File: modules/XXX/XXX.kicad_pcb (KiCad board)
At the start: 2 copper layers, 160 x 100 mm, 15 parts, among them J1 CardConnector, SW1 AS13AP, SW2 AS13AP, SW3 AS13AP

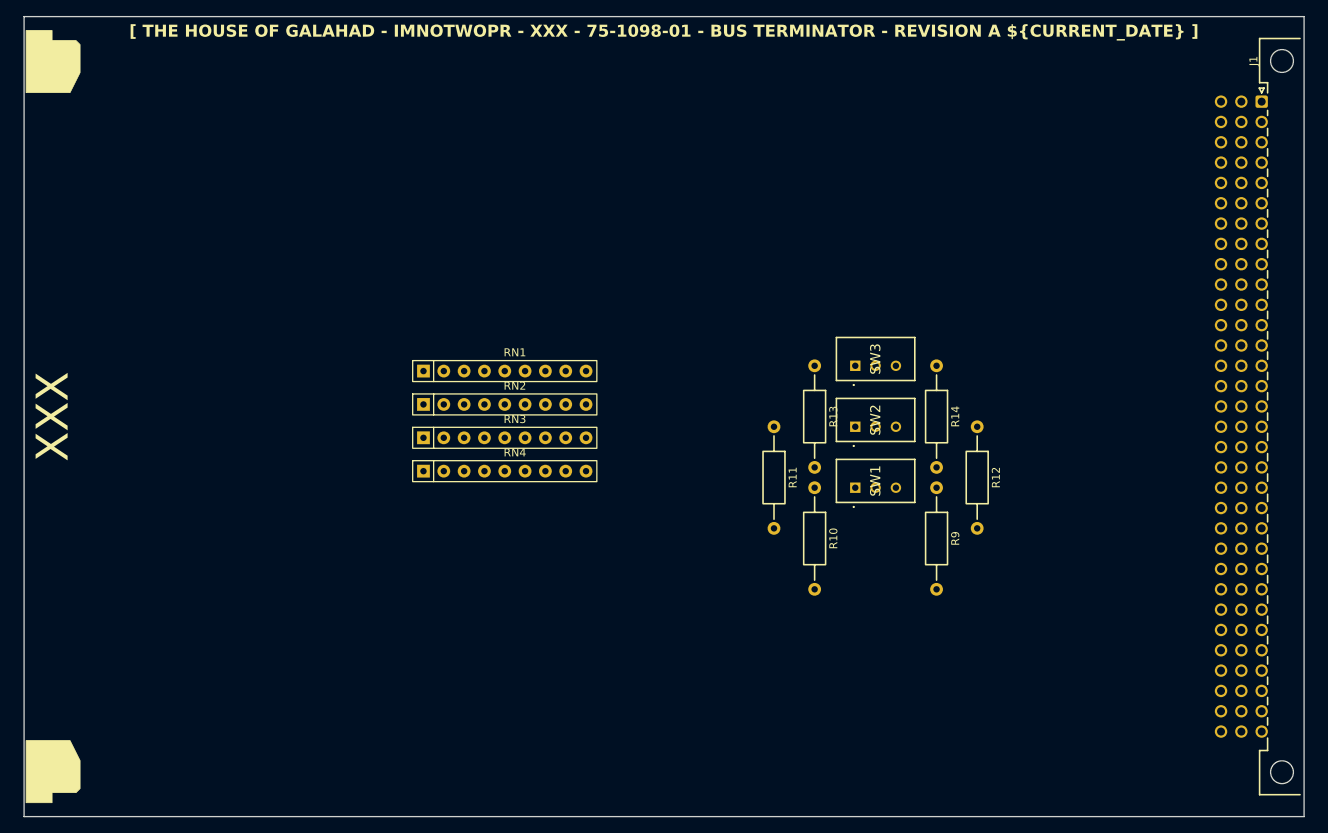
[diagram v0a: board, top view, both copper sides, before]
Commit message: fixed level shifter footprint width
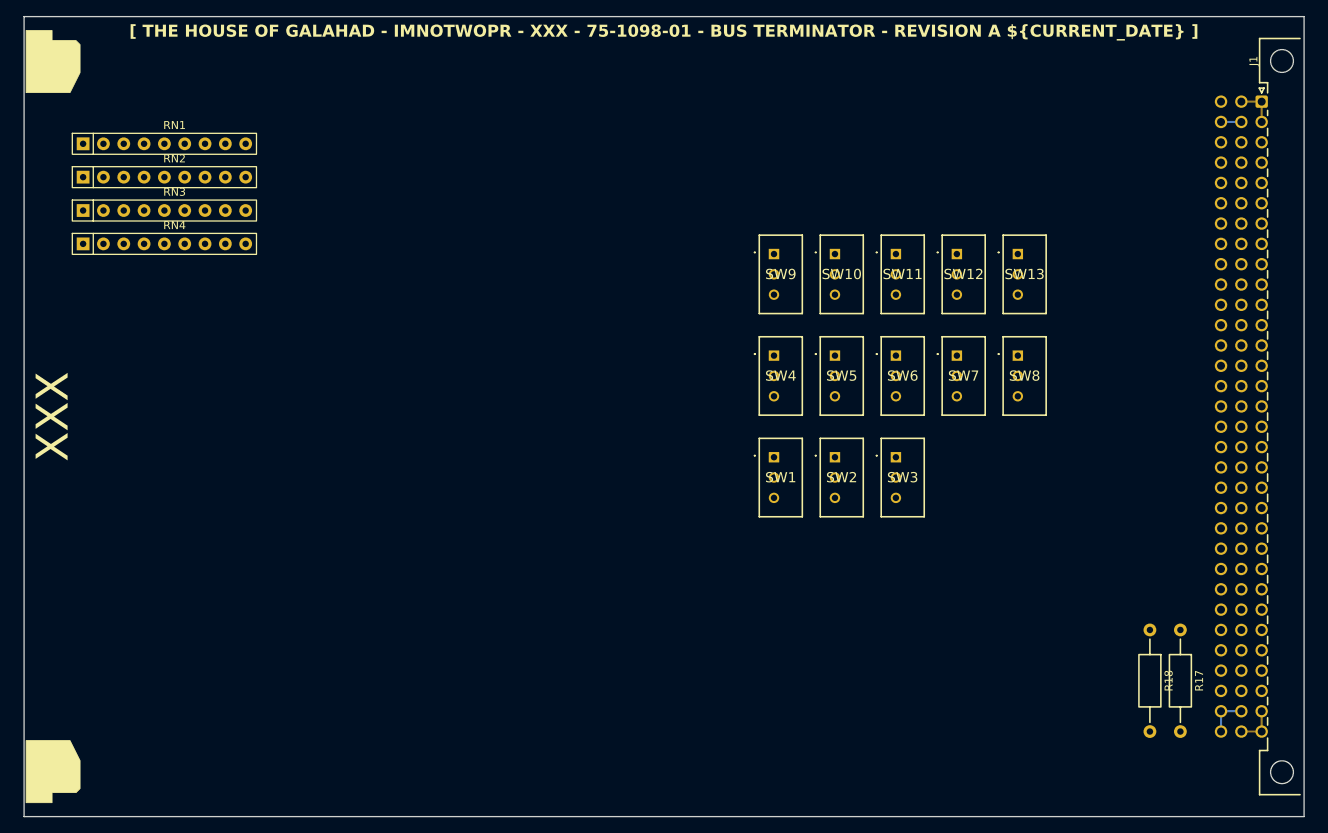
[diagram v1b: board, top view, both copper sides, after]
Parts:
- removed R10, R11, R12, R13, R14, R9: 10k, IMNOTWOPR:R_Axial_DIN0207_P400mil
- added R17: 10k, IMNOTWOPR:R_Axial_DIN0207_P400mil, F.Cu at (199.5, 128.0)
- added R18: 10k, IMNOTWOPR:R_Axial_DIN0207_P400mil, F.Cu at (195.7, 128.0)
- added SW10: AS13AP, IMNOTWOPR:AS13AP, F.Cu at (156.4, 74.7)
- added SW11: AS13AP, IMNOTWOPR:AS13AP, F.Cu at (164.0, 74.7)
- added SW12: AS13AP, IMNOTWOPR:AS13AP, F.Cu at (171.6, 74.7)
- added SW13: AS13AP, IMNOTWOPR:AS13AP, F.Cu at (179.2, 74.7)
- added SW4: AS13AP, IMNOTWOPR:AS13AP, F.Cu at (148.7, 87.4)
- added SW5: AS13AP, IMNOTWOPR:AS13AP, F.Cu at (156.4, 87.4)
- added SW6: AS13AP, IMNOTWOPR:AS13AP, F.Cu at (164.0, 87.4)
- added SW7: AS13AP, IMNOTWOPR:AS13AP, F.Cu at (171.6, 87.4)
- added SW8: AS13AP, IMNOTWOPR:AS13AP, F.Cu at (179.2, 87.4)
- added SW9: AS13AP, IMNOTWOPR:AS13AP, F.Cu at (148.7, 74.7)
- moved RN2 51.2 mm to (62.4, 65.1)
- moved RN3 51.2 mm to (62.4, 69.2)
- moved RN1 51.2 mm to (62.4, 60.9)
- moved RN4 51.2 mm to (62.4, 73.4)
- moved SW3 12.5 mm to (164.0, 100.1), turned to 0 degrees
- moved SW1 10.9 mm to (148.7, 100.1), turned to 0 degrees
- moved SW2 4.58 mm to (156.4, 100.1), turned to 0 degrees
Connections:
- J1 pad c10: unconnected-(J1C-BUSREQ3-Padc10) -> Net-(J1C-BUSREQ3)
- J1 pad c11: unconnected-(J1C-BUSREQ4-Padc11) -> Net-(J1C-BUSREQ4)
- J1 pad c13: unconnected-(J1C-BUSGNT0-Padc13) -> Net-(J1C-BUSGNT0)
- J1 pad c14: unconnected-(J1C-BUSGNT1-Padc14) -> Net-(J1C-BUSGNT1)
- J1 pad c15: unconnected-(J1C-BUSGNT2-Padc15) -> Net-(J1C-BUSGNT2)
- J1 pad c16: unconnected-(J1C-BUSGNT3-Padc16) -> Net-(J1C-BUSGNT3)
- J1 pad c17: unconnected-(J1C-BUSGNT4-Padc17) -> Net-(J1C-BUSGNT4)
- J1 pad c22: unconnected-(J1C-I^{2}C_SCL-Padc22) -> Net-(J1C-I^{2}C_SCL)
- J1 pad c23: unconnected-(J1C-I^{2}C_SDA-Padc23) -> Net-(J1C-I^{2}C_SDA)
- J1 pad c7: unconnected-(J1C-BUSREQ0-Padc7) -> Net-(J1C-BUSREQ0)
- J1 pad c8: unconnected-(J1C-BUSREQ1-Padc8) -> Net-(J1C-BUSREQ1)
- J1 pad c9: unconnected-(J1C-BUSREQ2-Padc9) -> Net-(J1C-BUSREQ2)
- SW1 pad 1: Net-(R10-Pad1) -> unconnected-(SW1-Pad1)
- SW1 pad 3: Net-(SW1-4) -> unconnected-(SW1-4-Pad3)
- SW2 pad 1: Net-(R11-Pad1) -> unconnected-(SW2-Pad1)
- SW2 pad 3: Net-(SW2-4) -> unconnected-(SW2-4-Pad3)
- SW3 pad 1: Net-(R13-Pad1) -> unconnected-(SW3-Pad1)
- SW3 pad 3: Net-(SW3-4) -> unconnected-(SW3-4-Pad3)
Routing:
- net +5V: track 0.00 -> 10.2 mm
- net GND: track 0.00 -> 7.62 mm

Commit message: xxx bus terminator card
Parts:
- removed R17, R18: 10k, IMNOTWOPR:R_Axial_DIN0207_P400mil
- removed RN4: 10k, Resistor_THT:R_Array_SIP9
- removed SW1, SW2, SW3, SW4, SW5, SW6, SW7, SW8: AS13AP, IMNOTWOPR:AS13AP
- added JP1: SDA_PU, IMNOTWOPR:Jumper_1x02, F.Cu at (164.0, 129.3)
- added JP2: SCL_PU, IMNOTWOPR:Jumper_1x02, F.Cu at (171.6, 129.3)
- added R1: 4k7, IMNOTWOPR:R_Axial_DIN0207_P400mil, F.Cu at (164.0, 117.9)
- added R2: 4k7, IMNOTWOPR:R_Axial_DIN0207_P400mil, F.Cu at (171.6, 115.3)
- added R3: 1k, IMNOTWOPR:R_Axial_DIN0207_P400mil, F.Cu at (158.9, 111.5)
- added R4: 1k, IMNOTWOPR:R_Axial_DIN0207_P400mil, F.Cu at (153.8, 120.4)
- added R5: 47k, IMNOTWOPR:R_Axial_DIN0207_P400mil, F.Cu at (161.4, 95.0)
- added R6: 47k, IMNOTWOPR:R_Axial_DIN0207_P400mil, F.Cu at (166.5, 97.5)
- added R7: 47k, IMNOTWOPR:R_Axial_DIN0207_P400mil, F.Cu at (171.6, 100.1)
- added RN6: 47k, Resistor_THT:R_Array_SIP6, F.Cu at (197.0, 106.4)
- added RN7: 47k, Resistor_THT:R_Array_SIP6, F.Cu at (197.0, 68.3)
- added RN8: 47k, Resistor_THT:R_Array_SIP6, F.Cu at (197.0, 83.6)
- RN1: value 10k -> 47k
- RN3: value 10k -> 4k7
- moved RN1 141.0 mm to (191.9, 116.6), turned to -90 degrees
- moved SW10 39.2 mm to (120.8, 58.2)
- moved SW11 39.2 mm to (128.4, 58.2)
- moved SW12 39.2 mm to (136.0, 58.2)
- moved SW13 39.2 mm to (143.7, 58.2)
- moved SW9 39.2 mm to (113.2, 58.2)
- moved RN2 26.3 mm to (88.1, 70.3)
- moved RN3 26.3 mm to (88.1, 74.4)
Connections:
- J1 pad a10: Net-(J1A-A_{14}) -> unconnected-(J1A-A_{14}-Pada10)
- J1 pad a11: Net-(J1A-A_{15}) -> unconnected-(J1A-A_{15}-Pada11)
- J1 pad a12: Net-(J1A-A_{16}) -> unconnected-(J1A-A_{16}-Pada12)
- J1 pad a13: Net-(J1A-A_{17}) -> unconnected-(J1A-A_{17}-Pada13)
- J1 pad a14: Net-(J1A-A_{18}) -> unconnected-(J1A-A_{18}-Pada14)
- J1 pad a15: Net-(J1A-A_{19}) -> unconnected-(J1A-A_{19}-Pada15)
- J1 pad a16: Net-(J1A-A_{20}) -> unconnected-(J1A-A_{20}-Pada16)
- J1 pad a17: Net-(J1A-A_{21}) -> unconnected-(J1A-A_{21}-Pada17)
- J1 pad a18: Net-(J1A-A_{22}) -> unconnected-(J1A-A_{22}-Pada18)
- J1 pad a19: Net-(J1A-A_{23}) -> unconnected-(J1A-A_{23}-Pada19)
- J1 pad a20: unconnected-(J1A-ABORT-Pada20) -> #ABORT
- J1 pad a25: unconnected-(J1A-HALT?-Pada25) -> #HALT
- J1 pad a26: unconnected-(J1A-IRQ_{4}-Pada26) -> #IRQ4
- J1 pad a27: unconnected-(J1A-IRQ_{5}-Pada27) -> #IRQ5
- J1 pad a28: unconnected-(J1A-IRQ_{6}-Pada28) -> #IRQ6
- J1 pad a29: unconnected-(J1A-IRQ_{7}-Pada29) -> #IRQ7
- J1 pad a4: Net-(J1A-A_{8}) -> unconnected-(J1A-A_{8}-Pada4)
- J1 pad a5: Net-(J1A-A_{9}) -> unconnected-(J1A-A_{9}-Pada5)
- J1 pad a6: Net-(J1A-A_{10}) -> unconnected-(J1A-A_{10}-Pada6)
- J1 pad a7: Net-(J1A-A_{11}) -> unconnected-(J1A-A_{11}-Pada7)
- J1 pad a8: Net-(J1A-A_{12}) -> unconnected-(J1A-A_{12}-Pada8)
- J1 pad a9: Net-(J1A-A_{13}) -> unconnected-(J1A-A_{13}-Pada9)
- J1 pad b10: Net-(J1B-A_{6}) -> unconnected-(J1B-A_{6}-Padb10)
- J1 pad b11: Net-(J1B-A_{7}) -> unconnected-(J1B-A_{7}-Padb11)
- J1 pad b12: unconnected-(J1B-RESET-Padb12) -> #RESET
- J1 pad b16: Net-(J1B-D_{0}) -> unconnected-(J1B-D_{0}-Padb16)
- J1 pad b17: Net-(J1B-D_{1}) -> unconnected-(J1B-D_{1}-Padb17)
- J1 pad b18: Net-(J1B-D_{2}) -> unconnected-(J1B-D_{2}-Padb18)
- J1 pad b19: Net-(J1B-D_{3}) -> unconnected-(J1B-D_{3}-Padb19)
- J1 pad b20: Net-(J1B-D_{4}) -> unconnected-(J1B-D_{4}-Padb20)
- J1 pad b21: Net-(J1B-D_{5}) -> unconnected-(J1B-D_{5}-Padb21)
- J1 pad b22: Net-(J1B-D_{6}) -> unconnected-(J1B-D_{6}-Padb22)
- J1 pad b23: Net-(J1B-D_{7}) -> unconnected-(J1B-D_{7}-Padb23)
- J1 pad b24: unconnected-(J1B-IRQ-Padb24) -> #IRQ
- J1 pad b25: unconnected-(J1B-NMI-Padb25) -> #NMI
- J1 pad b26: unconnected-(J1B-IRQ_{0}-Padb26) -> #IRQ0
- J1 pad b27: unconnected-(J1B-IRQ_{1}-Padb27) -> #IRQ1
- J1 pad b28: unconnected-(J1B-IRQ_{2}-Padb28) -> #IRQ2
- J1 pad b29: unconnected-(J1B-IRQ_{3}-Padb29) -> #IRQ3
- J1 pad b4: Net-(J1B-A_{0}) -> unconnected-(J1B-A_{0}-Padb4)
- J1 pad b5: Net-(J1B-A_{1}) -> unconnected-(J1B-A_{1}-Padb5)
- J1 pad b6: Net-(J1B-A_{2}) -> unconnected-(J1B-A_{2}-Padb6)
- J1 pad b7: Net-(J1B-A_{3}) -> unconnected-(J1B-A_{3}-Padb7)
- J1 pad b8: Net-(J1B-A_{4}) -> unconnected-(J1B-A_{4}-Padb8)
- J1 pad b9: Net-(J1B-A_{5}) -> unconnected-(J1B-A_{5}-Padb9)
- J1 pad c10: Net-(J1C-BUSREQ3) -> #BUSREQ3
- J1 pad c11: Net-(J1C-BUSREQ4) -> #BUSREQ4
- J1 pad c13: Net-(J1C-BUSGNT0) -> #BUSGNT0
- J1 pad c14: Net-(J1C-BUSGNT1) -> #BUSGNT1
- J1 pad c15: Net-(J1C-BUSGNT2) -> #BUSGNT2
- J1 pad c16: Net-(J1C-BUSGNT3) -> #BUSGNT3
- J1 pad c17: Net-(J1C-BUSGNT4) -> #BUSGNT4
- J1 pad c19: Net-(J1C-BANK0) -> #BANK0
- J1 pad c20: Net-(J1C-BANK1) -> #BANK1
- J1 pad c21: Net-(J1C-BANK2) -> #BANK2
- J1 pad c25: unconnected-(J1C-READY-Padc25) -> READY
- J1 pad c29: unconnected-(J1C-BE-Padc29) -> BE
- J1 pad c7: Net-(J1C-BUSREQ0) -> #BUSREQ0
- J1 pad c8: Net-(J1C-BUSREQ1) -> #BUSREQ1
- J1 pad c9: Net-(J1C-BUSREQ2) -> #BUSREQ2
- RN1 pad 1: Net-(RN1-common) -> +5V
- RN1 pad 2: Net-(J1A-A_{8}) -> #IRQ0
- RN1 pad 3: Net-(J1A-A_{9}) -> #IRQ4
- RN1 pad 4: Net-(J1A-A_{10}) -> #IRQ1
- RN1 pad 5: Net-(J1A-A_{11}) -> #IRQ5
- RN1 pad 6: Net-(J1A-A_{12}) -> #IRQ2
- RN1 pad 7: Net-(J1A-A_{13}) -> #IRQ6
- RN1 pad 8: Net-(J1A-A_{14}) -> #IRQ3
- RN1 pad 9: Net-(J1A-A_{15}) -> #IRQ7
- RN2 pad 1: Net-(RN1-common) -> +5V
- RN2 pad 2: Net-(J1A-A_{16}) -> unconnected-(RN2-R1-Pad2)
- RN2 pad 3: Net-(J1A-A_{17}) -> unconnected-(RN2-R2-Pad3)
- RN2 pad 4: Net-(J1A-A_{18}) -> unconnected-(RN2-R3-Pad4)
- RN2 pad 5: Net-(J1A-A_{19}) -> unconnected-(RN2-R4-Pad5)
- RN2 pad 6: Net-(J1A-A_{20}) -> unconnected-(RN2-R5-Pad6)
- RN2 pad 7: Net-(J1A-A_{21}) -> unconnected-(RN2-R6-Pad7)
- RN2 pad 8: Net-(J1A-A_{22}) -> unconnected-(RN2-R7-Pad8)
- RN2 pad 9: Net-(J1A-A_{23}) -> unconnected-(RN2-R8-Pad9)
- RN3 pad 1: Net-(RN1-common) -> GND
- RN3 pad 2: Net-(J1B-A_{0}) -> unconnected-(RN3-R1-Pad2)
- RN3 pad 3: Net-(J1B-A_{1}) -> unconnected-(RN3-R2-Pad3)
- RN3 pad 4: Net-(J1B-A_{2}) -> unconnected-(RN3-R3-Pad4)
- RN3 pad 5: Net-(J1B-A_{3}) -> unconnected-(RN3-R4-Pad5)
- RN3 pad 6: Net-(J1B-A_{4}) -> unconnected-(RN3-R5-Pad6)
- RN3 pad 7: Net-(J1B-A_{5}) -> unconnected-(RN3-R6-Pad7)
- RN3 pad 8: Net-(J1B-A_{6}) -> unconnected-(RN3-R7-Pad8)
- RN3 pad 9: Net-(J1B-A_{7}) -> unconnected-(RN3-R8-Pad9)
- SW10 pad 2: Net-(J1C-BUSREQ1) -> unconnected-(SW10-3-Pad2)
- SW11 pad 2: Net-(J1C-BUSREQ2) -> unconnected-(SW11-3-Pad2)
- SW12 pad 2: Net-(J1C-BUSREQ3) -> unconnected-(SW12-3-Pad2)
- SW13 pad 2: Net-(J1C-BUSREQ4) -> unconnected-(SW13-3-Pad2)
- SW9 pad 2: Net-(J1C-BUSREQ0) -> unconnected-(SW9-3-Pad2)
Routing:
- net #RESET: track 0.00 -> 30.7 mm
- net #IRQ7: track 0.00 -> 22.0 mm
- net #IRQ6: track 0.00 -> 20.9 mm
- net #IRQ5: track 0.00 -> 19.9 mm
- net #IRQ4: track 0.00 -> 18.8 mm
- net #IRQ3: track 0.00 -> 18.4 mm
- net #IRQ2: track 0.00 -> 17.3 mm
- net #IRQ1: track 0.00 -> 16.3 mm
- net #IRQ0: track 0.00 -> 16.3 mm
- net #ABORT: track 0.00 -> 15.9 mm
- net #HALT: track 0.00 -> 13.8 mm
- net #NMI: track 0.00 -> 11.2 mm
- net #IRQ: track 0.00 -> 11.2 mm
- net #BUSREQ4: track 0.00 -> 7.62 mm
- net #BUSREQ3: track 0.00 -> 7.62 mm
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
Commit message: pxx prototype card
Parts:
- removed SW10, SW11, SW12, SW13, SW9: AS13AP, IMNOTWOPR:AS13AP
- added SW1: SW_SPDT_MSM, IMNOTWOPR:AS13AP, F.Cu at (94.1, 68.3)
- added SW2: SW_SPDT_MSM, IMNOTWOPR:AS13AP, F.Cu at (104.3, 68.3)
- added SW3: SW_SPDT_MSM, IMNOTWOPR:AS13AP, F.Cu at (114.5, 68.3)
- added SW4: SW_SPDT_MSM, IMNOTWOPR:AS13AP, F.Cu at (94.1, 116.6)
- added SW5: SW_SPDT_MSM, IMNOTWOPR:AS13AP, F.Cu at (104.3, 116.6)
- added SW6: SW_SPDT_MSM, IMNOTWOPR:AS13AP, F.Cu at (114.5, 116.6)
- added SW7: SW_SPDT_MSM, IMNOTWOPR:AS13AP, F.Cu at (124.6, 116.6)
- added SW8: SW_SPDT_MSM, IMNOTWOPR:AS13AP, F.Cu at (134.8, 116.6)
- moved RN2 37.4 mm to (106.8, 102.6)
- moved R4 34.1 mm to (177.9, 96.3)
- moved RN3 25.1 mm to (106.8, 91.2)
- moved R3 21.6 mm to (174.1, 96.3)
- moved R5 20.4 mm to (181.8, 96.3)
- moved R6 19.1 mm to (185.6, 96.3)
- moved R7 18.2 mm to (189.4, 96.3)
- moved JP1 14.0 mm to (177.9, 130.6)
- moved R1 14.0 mm to (177.9, 119.1)
- moved R2 13.3 mm to (184.3, 119.1)
- moved JP2 12.8 mm to (184.3, 130.6)
- moved RN6 7.62 mm to (197.0, 98.8)
- moved RN1 5.68 mm to (197.0, 114.0)
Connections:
- RN2 pad 2: unconnected-(RN2-R1-Pad2) -> Net-(RN2-R1)
- RN2 pad 3: unconnected-(RN2-R2-Pad3) -> Net-(RN2-R2)
- RN2 pad 4: unconnected-(RN2-R3-Pad4) -> Net-(RN2-R3)
- RN2 pad 5: unconnected-(RN2-R4-Pad5) -> Net-(RN2-R4)
- RN2 pad 6: unconnected-(RN2-R5-Pad6) -> Net-(RN2-R5)
- RN2 pad 7: unconnected-(RN2-R6-Pad7) -> Net-(RN2-R6)
- RN2 pad 8: unconnected-(RN2-R7-Pad8) -> Net-(RN2-R7)
- RN2 pad 9: unconnected-(RN2-R8-Pad9) -> Net-(RN2-R8)
- RN3 pad 2: unconnected-(RN3-R1-Pad2) -> Net-(RN3-R1)
- RN3 pad 3: unconnected-(RN3-R2-Pad3) -> Net-(RN3-R2)
- RN3 pad 4: unconnected-(RN3-R3-Pad4) -> Net-(RN3-R3)
- RN3 pad 5: unconnected-(RN3-R4-Pad5) -> Net-(RN3-R4)
- RN3 pad 6: unconnected-(RN3-R5-Pad6) -> Net-(RN3-R5)
- RN3 pad 7: unconnected-(RN3-R6-Pad7) -> Net-(RN3-R6)
- RN3 pad 8: unconnected-(RN3-R7-Pad8) -> Net-(RN3-R7)
- RN3 pad 9: unconnected-(RN3-R8-Pad9) -> Net-(RN3-R8)
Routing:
- net +5V: track 10.2 -> 311.9 mm
- net GND: track 7.62 -> 157.3 mm
- net BE: track 0.00 -> 67.8 mm
- net Net-(RN3-R4): track 0.00 -> 57.7 mm
- net Net-(RN2-R1): track 0.00 -> 53.9 mm
- net Net-(RN3-R5): track 0.00 -> 50.1 mm
- net Net-(RN2-R2): track 0.00 -> 46.2 mm
- net READY: track 0.00 -> 43.7 mm
- net Net-(RN3-R6): track 0.00 -> 42.4 mm
- net Net-(RN3-R8): track 0.00 -> 39.2 mm
- net Net-(RN2-R3): track 0.00 -> 38.6 mm
- net Net-(RN2-R4): track 0.00 -> 36.8 mm
- net Net-(RN3-R1): track 0.00 -> 33.0 mm
- net Net-(RN3-R7): track 0.00 -> 31.5 mm
- net Net-(J1C-I^{2}C_SDA): track 0.00 -> 29.3 mm
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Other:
- board text added: "BUS GRANT OVERRIDE"
- board text added: "HIGH AUTO LOW"
- board text added: "MEMORY MAP OVERRIDE"

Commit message: work on RAM and bus terminator
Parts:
- removed RN2: 10k, Resistor_THT:R_Array_SIP9
- removed RN3: 4k7, Resistor_THT:R_Array_SIP9
- added R10: 10k, IMNOTWOPR:R_Axial_DIN0207_P400mil, F.Cu at (110.6, 60.7)
- added R11: 10k, IMNOTWOPR:R_Axial_DIN0207_P400mil, F.Cu at (87.8, 109.0)
- added R12: 10k, IMNOTWOPR:R_Axial_DIN0207_P400mil, F.Cu at (99.2, 109.0)
- added R13: 10k, IMNOTWOPR:R_Axial_DIN0207_P400mil, F.Cu at (110.6, 109.0)
- added R14: 10k, IMNOTWOPR:R_Axial_DIN0207_P400mil, F.Cu at (122.1, 109.0)
- added R15: 10k, IMNOTWOPR:R_Axial_DIN0207_P400mil, F.Cu at (133.5, 109.0)
- added R16: 4k7, IMNOTWOPR:R_Axial_DIN0207_P400mil, F.Cu at (87.8, 78.5)
- added R17: 4k7, IMNOTWOPR:R_Axial_DIN0207_P400mil, F.Cu at (99.2, 78.5)
- added R18: 4k7, IMNOTWOPR:R_Axial_DIN0207_P400mil, F.Cu at (110.6, 78.5)
- added R19: 4k7, IMNOTWOPR:R_Axial_DIN0207_P400mil, F.Cu at (87.8, 126.8)
- added R20: 4k7, IMNOTWOPR:R_Axial_DIN0207_P400mil, F.Cu at (99.2, 126.8)
- added R21: 4k7, IMNOTWOPR:R_Axial_DIN0207_P400mil, F.Cu at (110.6, 126.8)
- added R22: 4k7, IMNOTWOPR:R_Axial_DIN0207_P400mil, F.Cu at (122.1, 126.8)
- added R23: 4k7, IMNOTWOPR:R_Axial_DIN0207_P400mil, F.Cu at (133.5, 126.8)
- added R8: 10k, IMNOTWOPR:R_Axial_DIN0207_P400mil, F.Cu at (87.8, 60.7)
- added R9: 10k, IMNOTWOPR:R_Axial_DIN0207_P400mil, F.Cu at (99.2, 60.7)
- moved SW4 12.8 mm to (81.4, 115.3)
- moved SW1 12.8 mm to (81.4, 67.1)
- moved SW5 11.5 mm to (92.9, 115.3)
- moved SW2 11.5 mm to (92.9, 67.1)
- moved SW6 10.2 mm to (104.3, 115.3)
- moved SW3 10.2 mm to (104.3, 67.1)
- moved SW7 8.98 mm to (115.7, 115.3)
- moved SW8 7.73 mm to (127.2, 115.3)
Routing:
- net GND: track 157.3 -> 305.2 mm
- net +5V: track 311.9 -> 418.0 mm
- net #BANK0: track 24.4 -> 115.7 mm, vias 0 -> 1
- net #BUSGNT0: track 7.62 -> 95.1 mm
- net #BUSGNT1: track 7.62 -> 88.8 mm
- net #BANK1: track 20.6 -> 99.7 mm, vias 0 -> 2
- net #BUSGNT2: track 7.62 -> 77.3 mm
- net #BANK2: track 16.8 -> 83.2 mm
- net #BUSGNT3: track 7.62 -> 66.7 mm
- net Net-(SW4-4): track 57.7 -> 6.35 mm
- net #BUSGNT4: track 7.62 -> 55.2 mm
- net Net-(R8-Pad1): track 53.9 -> 6.35 mm
- net Net-(SW5-4): track 50.1 -> 6.35 mm
- net Net-(R9-Pad1): track 46.2 -> 6.35 mm
- net Net-(SW6-4): track 42.4 -> 6.35 mm
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
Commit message: terminator card work
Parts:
- removed RN1: 47k, Resistor_THT:R_Array_SIP9
- removed RN6, RN7, RN8: 47k, Resistor_THT:R_Array_SIP6
- added R24: 47k, IMNOTWOPR:R_Axial_DIN0207_P400mil, F.Cu at (193.2, 83.6)
- added R25: 47k, IMNOTWOPR:R_Axial_DIN0207_P400mil, F.Cu at (175.4, 103.9)
- added R26: 47k, IMNOTWOPR:R_Axial_DIN0207_P400mil, F.Cu at (193.2, 114.0)
- added R27: 47k, IMNOTWOPR:R_Axial_DIN0207_P400mil, F.Cu at (193.2, 116.6)
- added R28: 47k, IMNOTWOPR:R_Axial_DIN0207_P400mil, F.Cu at (175.4, 116.6)
- added R29: 47k, IMNOTWOPR:R_Axial_DIN0207_P400mil, F.Cu at (193.2, 119.1)
- added R30: 47k, IMNOTWOPR:R_Axial_DIN0207_P400mil, F.Cu at (175.4, 119.1)
- added R31: 47k, IMNOTWOPR:R_Axial_DIN0207_P400mil, F.Cu at (193.2, 121.7)
- added R32: 47k, IMNOTWOPR:R_Axial_DIN0207_P400mil, F.Cu at (175.4, 121.7)
- added R33: 47k, IMNOTWOPR:R_Axial_DIN0207_P400mil, F.Cu at (193.2, 124.2)
- added R34: 47k, IMNOTWOPR:R_Axial_DIN0207_P400mil, F.Cu at (175.4, 124.2)
- added R35: 47k, IMNOTWOPR:R_Axial_DIN0207_P400mil, F.Cu at (193.2, 126.8)
- added R36: 47k, IMNOTWOPR:R_Axial_DIN0207_P400mil, F.Cu at (175.4, 126.8)
- added R37: 47k, IMNOTWOPR:R_Axial_DIN0207_P400mil, F.Cu at (193.2, 70.9)
- added R38: 47k, IMNOTWOPR:R_Axial_DIN0207_P400mil, F.Cu at (193.2, 73.4)
- added R39: 47k, IMNOTWOPR:R_Axial_DIN0207_P400mil, F.Cu at (193.2, 76.0)
- added R40: 47k, IMNOTWOPR:R_Axial_DIN0207_P400mil, F.Cu at (193.2, 78.5)
- added R41: 47k, IMNOTWOPR:R_Axial_DIN0207_P400mil, F.Cu at (193.2, 81.0)
- added R42: 47k, IMNOTWOPR:R_Axial_DIN0207_P400mil, F.Cu at (193.2, 86.1)
- added R43: 47k, IMNOTWOPR:R_Axial_DIN0207_P400mil, F.Cu at (193.2, 88.7)
- added R44: 47k, IMNOTWOPR:R_Axial_DIN0207_P400mil, F.Cu at (193.2, 91.2)
- added R45: 47k, IMNOTWOPR:R_Axial_DIN0207_P400mil, F.Cu at (193.2, 93.7)
- added R46: 47k, IMNOTWOPR:R_Axial_DIN0207_P400mil, F.Cu at (193.2, 96.3)
- moved R4 36.4 mm to (193.2, 129.3), turned to 180 degrees
- moved R3 33.0 mm to (175.4, 129.3), turned to 180 degrees
- moved JP2 21.7 mm to (181.8, 109.0), turned to -90 degrees
- moved JP1 19.4 mm to (181.8, 111.5), turned to -90 degrees
- moved R1 17.0 mm to (193.2, 111.5), turned to 180 degrees
- moved R2 13.5 mm to (193.2, 109.0), turned to 180 degrees
- moved R5 12.5 mm to (193.2, 101.3), turned to 180 degrees
- moved R7 10.9 mm to (193.2, 106.4), turned to 180 degrees
- moved R6 10.8 mm to (193.2, 103.9), turned to 180 degrees
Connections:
- J1 pad a3: +12V -> unconnected-(J1A-+12V-Pada3)
- J1 pad a30: +12V -> unconnected-(J1A-+12V-Pada30)
- J1 pad b3: -12V -> unconnected-(J1B--12V-Padb3)
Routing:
- net #BUSGNT0: track 95.1 -> 154.2 mm, vias 0 -> 1
- net #BANK2: track 83.2 -> 135.2 mm, vias 0 -> 1
- net #BUSGNT1: track 88.8 -> 140.2 mm, vias 0 -> 1
- net #BUSGNT2: track 77.3 -> 126.3 mm, vias 0 -> 1
- net GND: track 305.2 -> 352.5 mm
- net #BUSGNT3: track 66.7 -> 112.3 mm, vias 0 -> 1
- net #BANK1: track 99.7 -> 144.9 mm, vias 2 -> 1
- net #BUSGNT4: track 55.2 -> 98.3 mm, vias 0 -> 1
- net BE: track 54.4 -> 13.0 mm, vias 1 -> 0
- net #BANK0: track 115.7 -> 154.5 mm
- net +5V: track 418.0 -> 450.2 mm
- net #RESET: track 39.2 -> 8.67 mm
- net Net-(J1C-I^{2}C_SDA): track 29.3 -> 5.08 mm
- net Net-(J1C-I^{2}C_SCL): track 23.0 -> 5.08 mm
- net #IRQ: track 26.5 -> 8.67 mm
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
